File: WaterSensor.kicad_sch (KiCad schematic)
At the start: 8 parts, among them J2 Conn_01x03_Pin, Q1 2N3904

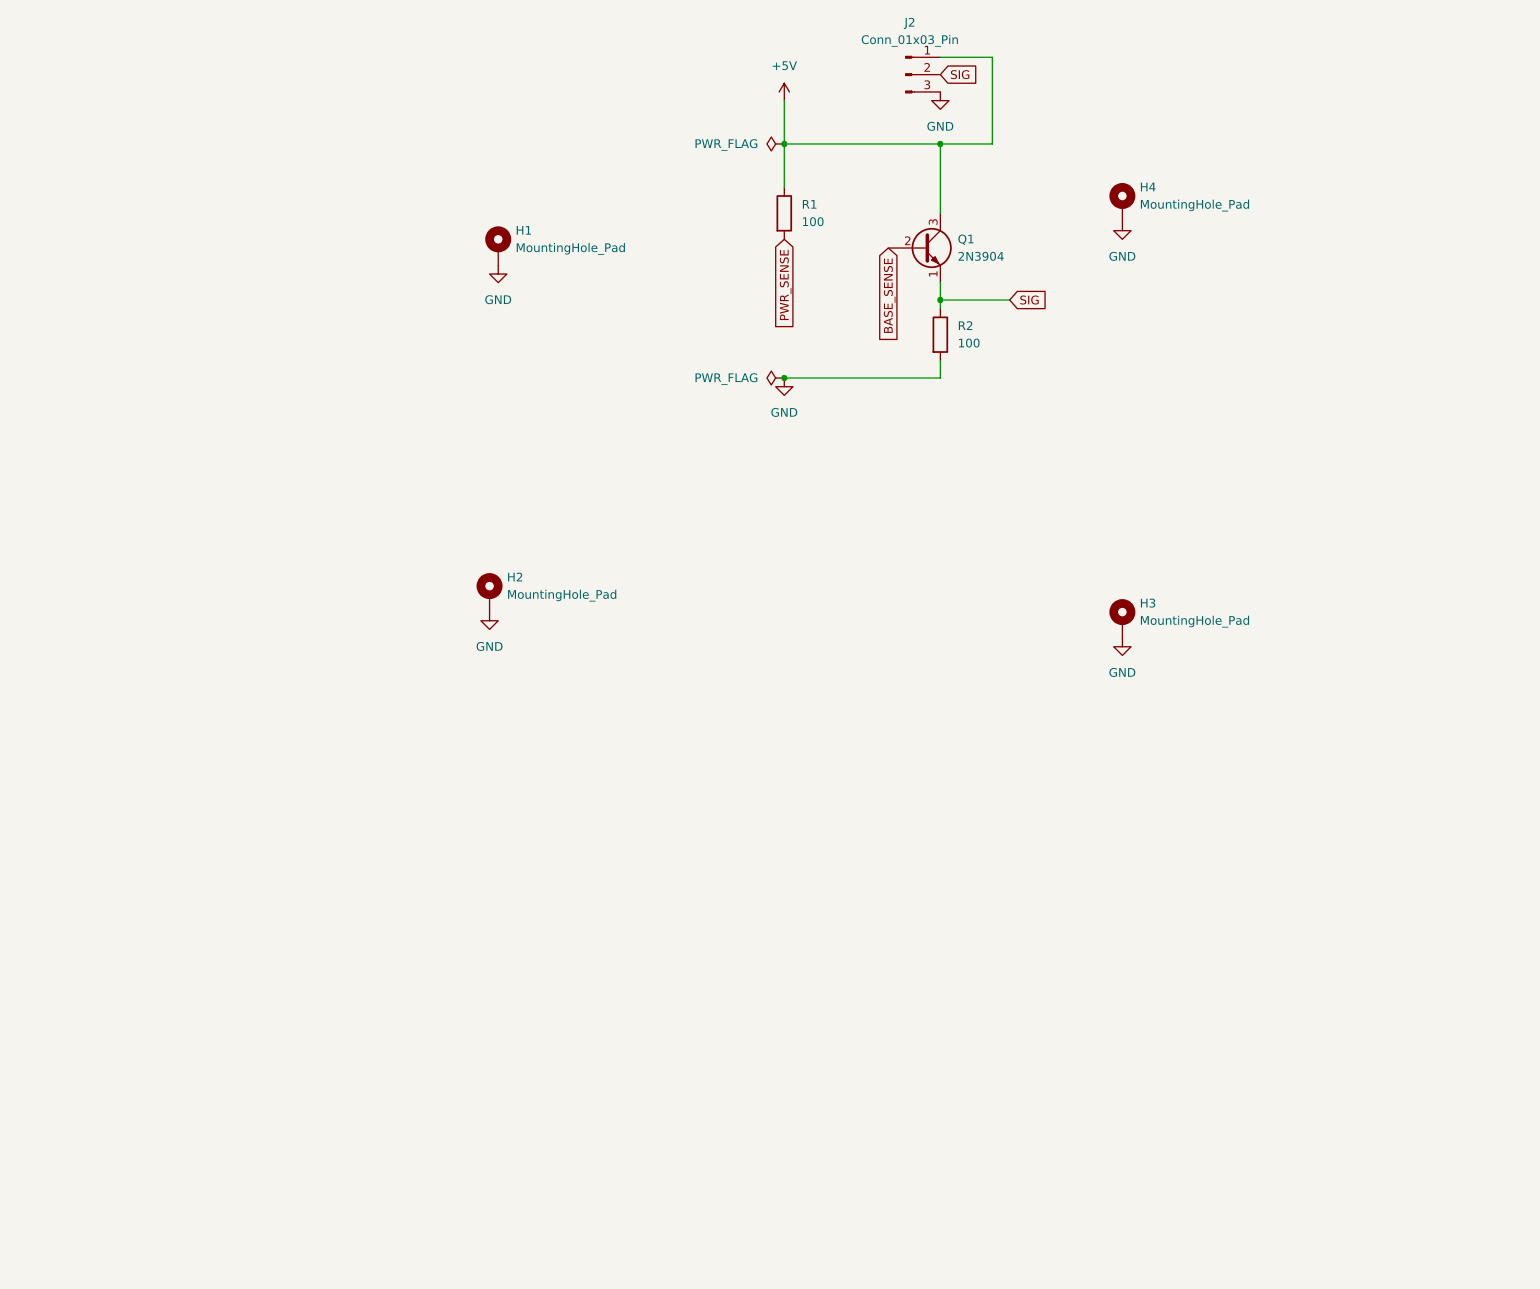
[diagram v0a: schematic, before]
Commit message: General cleanup of schematic and PCB
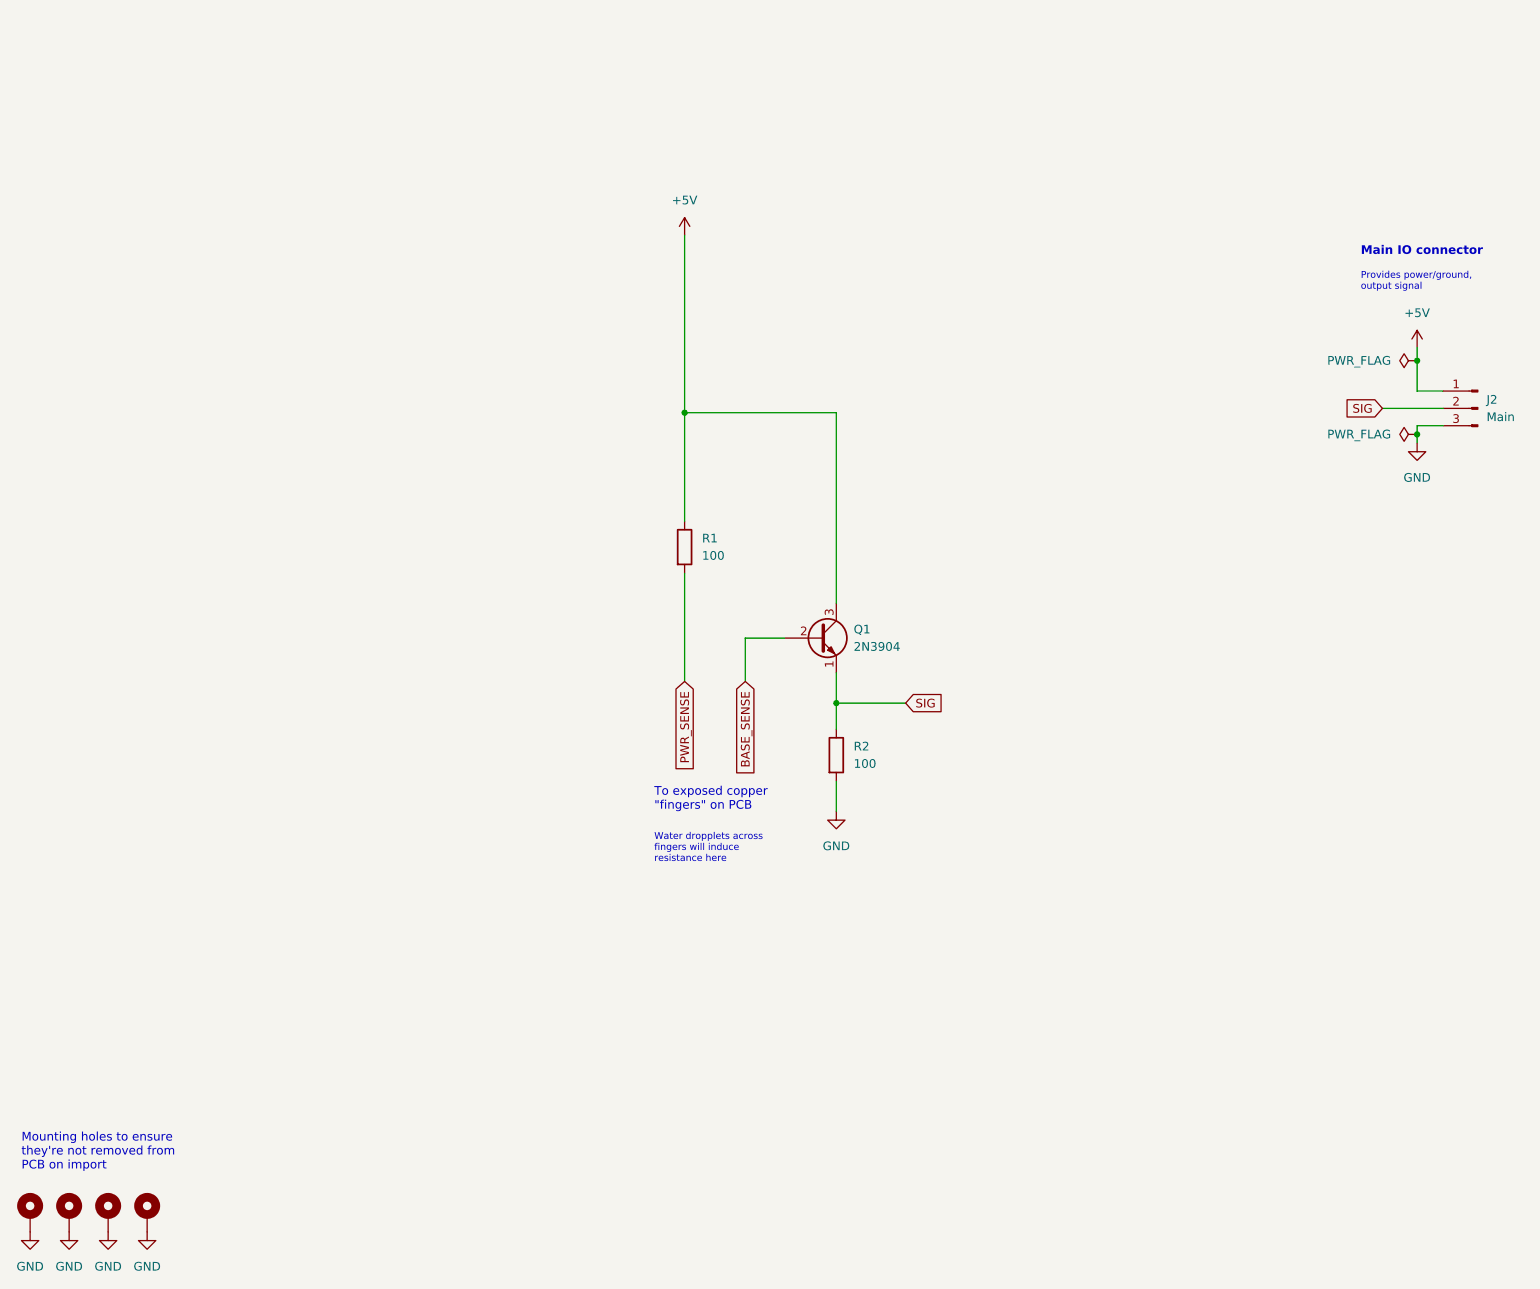
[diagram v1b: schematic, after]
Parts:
- J2: value Conn_01x03_Pin -> Main
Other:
- note added: "Main IO connector"
- note added: "Mounting holes to ensure they're not removed from PCB on import"
- note added: "Provides power/ground, output signal"
- note added: "To exposed copper "fingers" on PCB"
- note added: "Water dropplets across fingers will induce resistance here"
- title: (none) -> Water Sensor
- moved on the sheet: J2, Q1, R1, R2

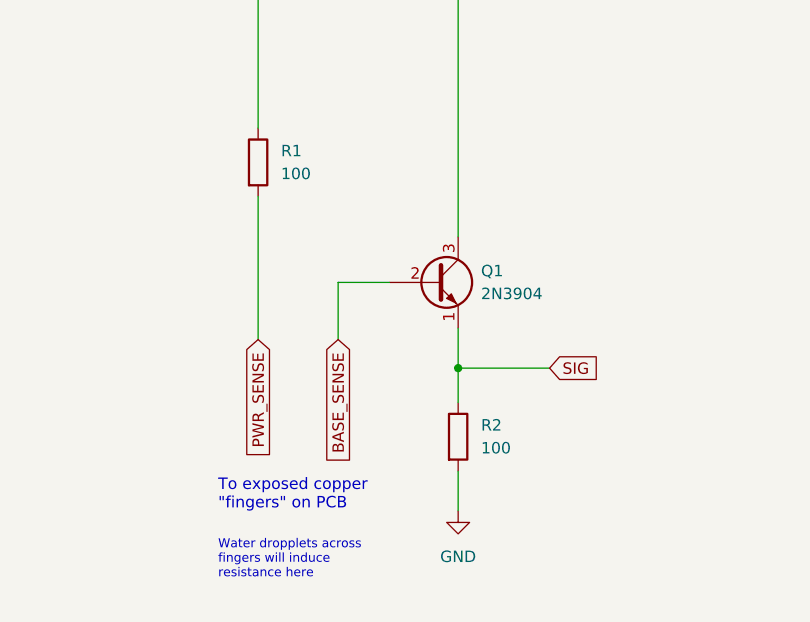
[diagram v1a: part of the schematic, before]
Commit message: Update resistor values based on calculations in README
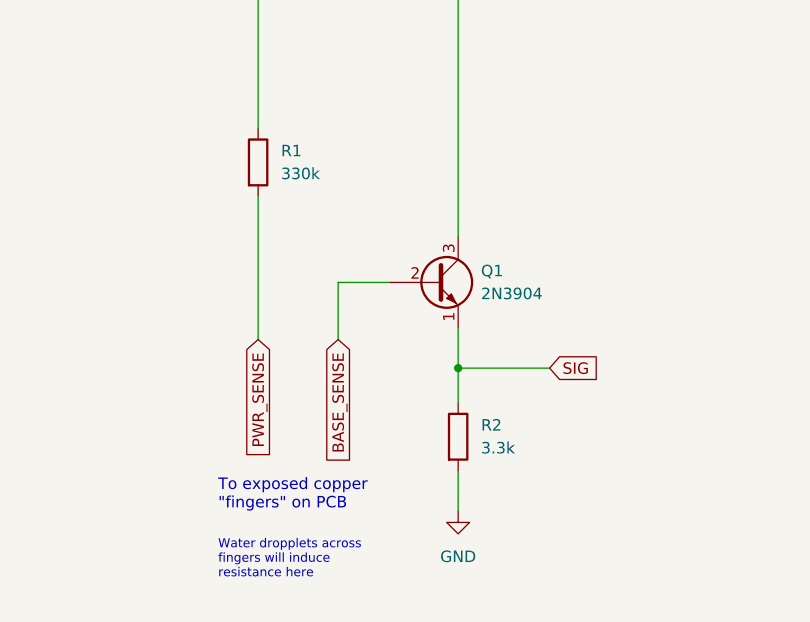
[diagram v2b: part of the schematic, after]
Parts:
- R1: value 100 -> 330k
- R2: value 100 -> 3.3k
